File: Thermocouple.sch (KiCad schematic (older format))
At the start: 0 parts

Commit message: Module 2, Unit 13 Defining Your Inputs and Outputs
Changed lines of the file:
@@
 $Descr A4 11693 8268
 encoding utf-8
-Sheet 3 8
+Sheet 8 8
 Title ""
 Date ""
@@
 Comment4 ""
 $EndDescr
-Text HLabel 9450 2850 2    60   Input ~ 0
+Text HLabel 9400 2750 2    60   Input ~ 0
 TC IN +
-Text HLabel 9450 3150 2    60   Input ~ 0
+Text HLabel 9400 3050 2    60   Input ~ 0
 TC IN -
+Text HLabel 2150 1650 0    60   Input ~ 0
+MOSI
+Text HLabel 2150 1950 0    60   Output ~ 0
+MISO
+Text HLabel 2150 2250 0    60   Input ~ 0
+SCLK
+Text HLabel 2150 2600 0    60   Input ~ 0
+CS_N
 $EndSCHEMATC

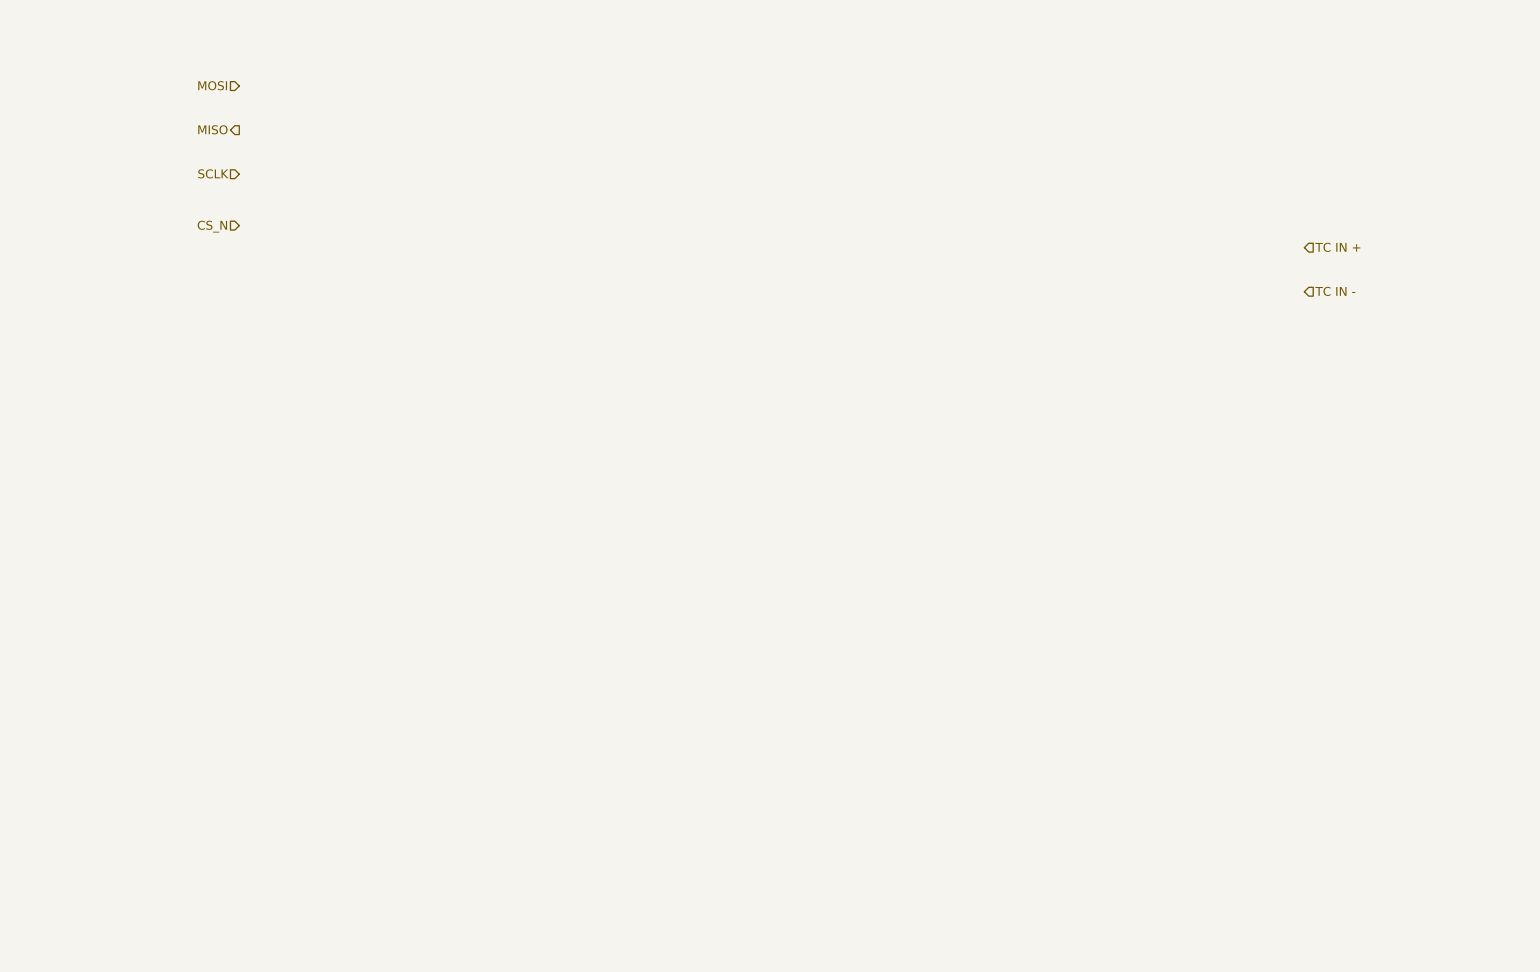
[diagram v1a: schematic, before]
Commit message: 3.3 Thermocouple Module - Initial Design
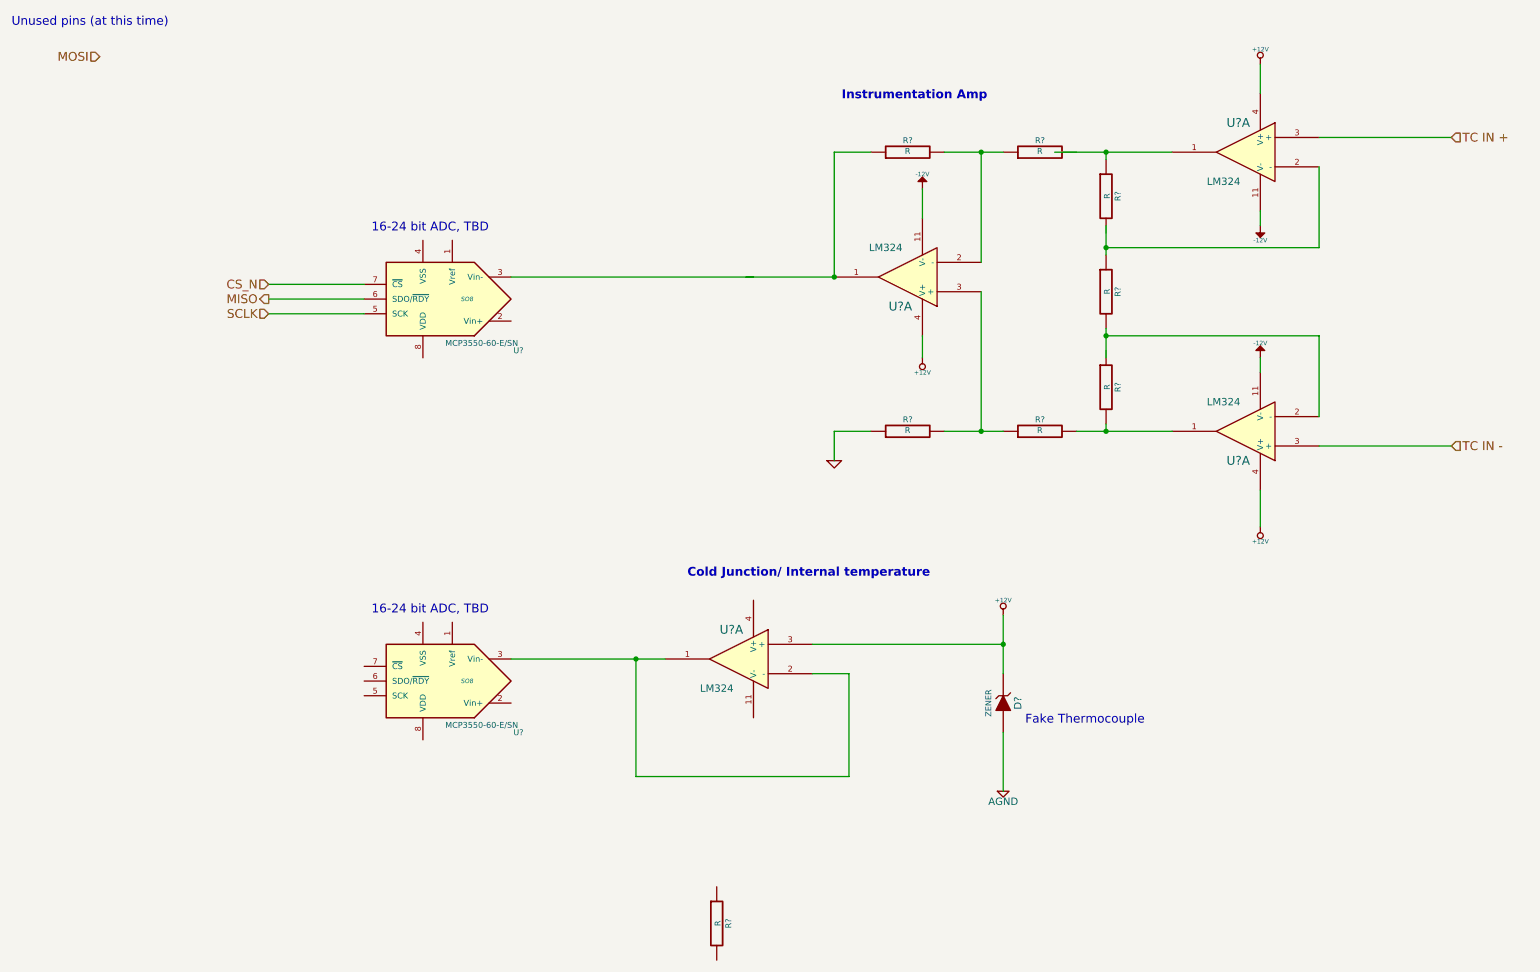
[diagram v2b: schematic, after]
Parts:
- added D?: ZENER, symbol ZENER
- added R? (x8): R, symbol R
- added U? (x4): LM324, symbol LM324
- added U? (x2): MCP3550-60-E/SN, SO8, symbol MCP3550-60-E/SN
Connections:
- net labels added: +12V, -12V, AGND, GND
- wire segments 0 -> 39
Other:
- note added: "16-24 bit ADC, TBD"
- note added: "Cold Junction/ Internal temperature"
- note added: "Fake Thermocouple"
- note added: "Instrumentation Amp"
- note added: "Unused pins (at this time)\n"
